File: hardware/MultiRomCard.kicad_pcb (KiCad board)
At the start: 2 copper layers, 125 x 100 mm, 22 parts, among them P1 VC4000_Cartridge_Bus, P2 MicroSD_Breakout, U1 Arduino_Nano, U10 74HC32, U2 74HC595, U3 74HC595, U4 74HC595, U5 6264, U6 74HC245, U7 74HC245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

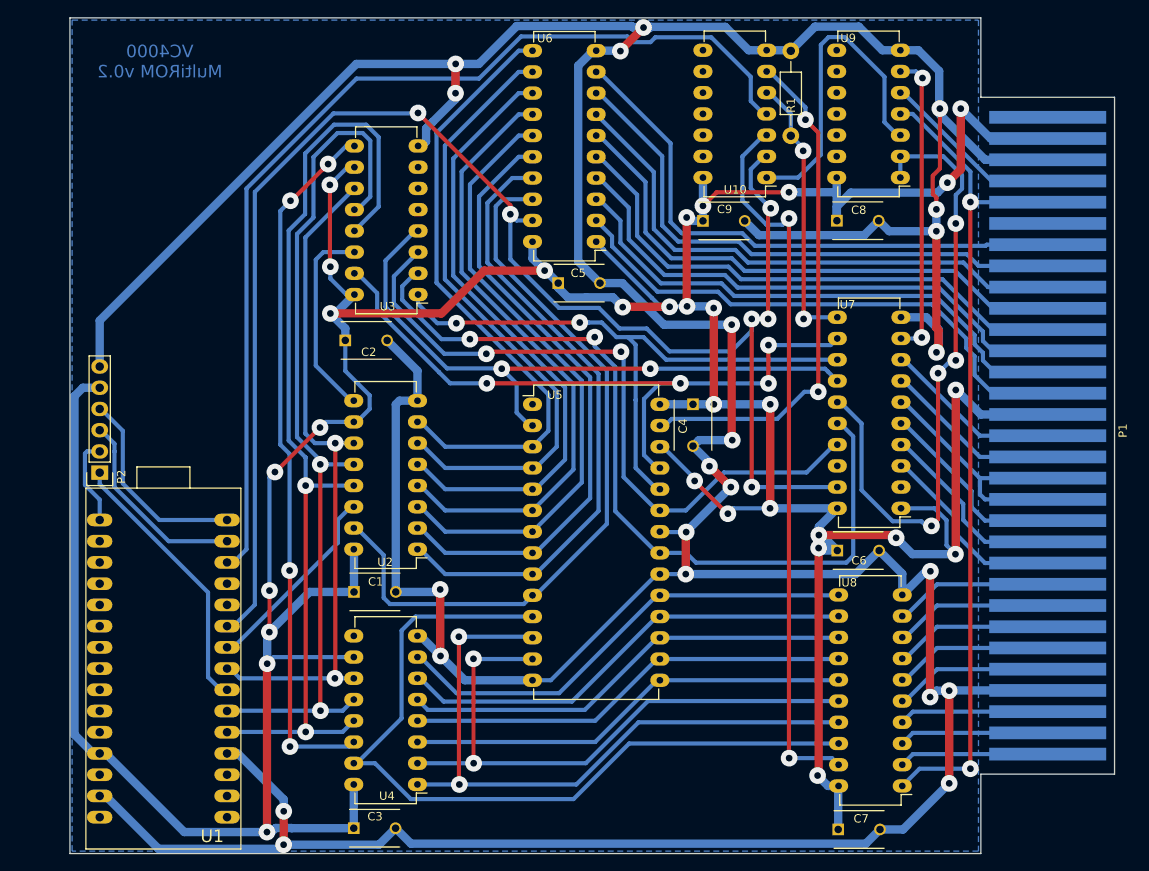
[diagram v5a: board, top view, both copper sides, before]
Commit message: added 3 push buttons and a display prot connected to I2C
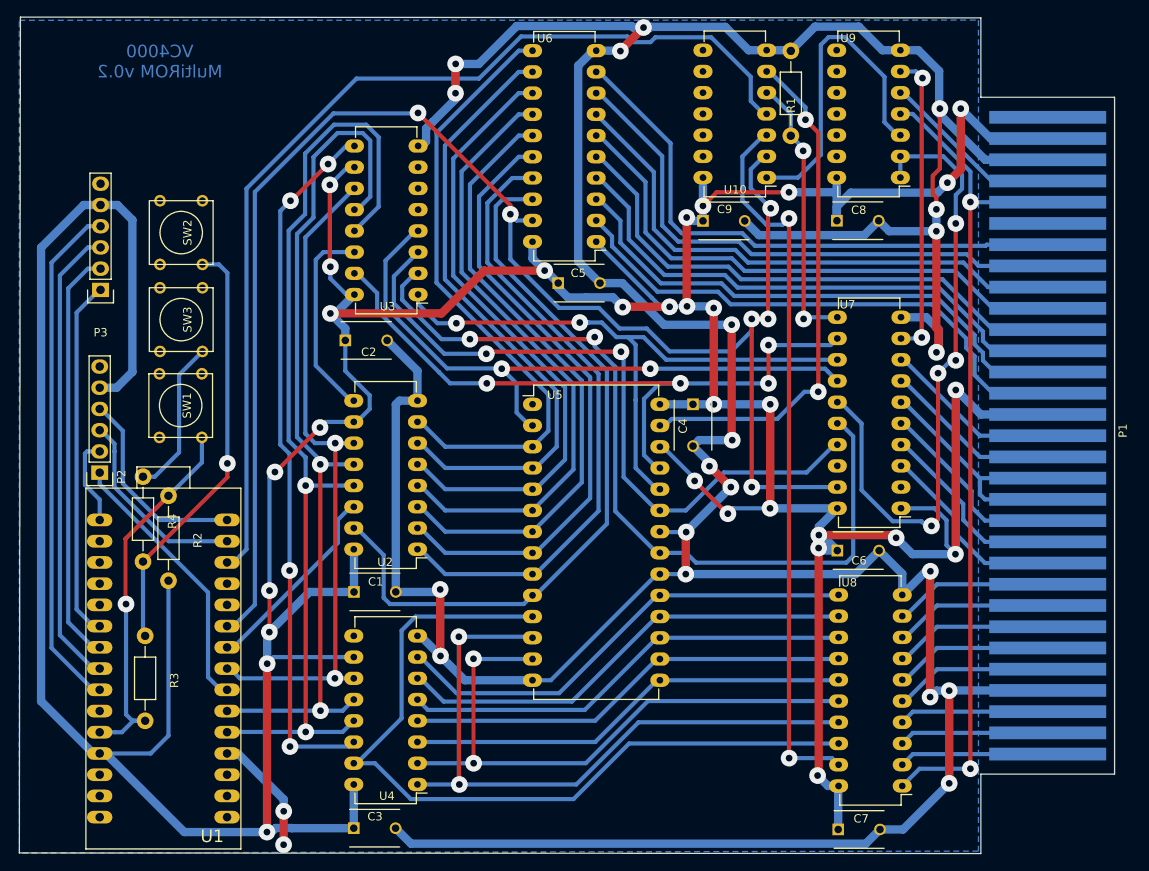
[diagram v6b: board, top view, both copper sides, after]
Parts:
- added P3: DISPLAY, Pin_Headers:Pin_Header_Straight_1x06, F.Cu at (89.7, 81.1)
- added R2: 2k2, Resistors_ThroughHole:Resistor_Horizontal_RM10mm, F.Cu at (97.8, 110.8)
- added R3: 330, Resistors_ThroughHole:Resistor_Horizontal_RM10mm, F.Cu at (95.0, 127.5)
- added R4: 1k, Resistors_ThroughHole:Resistor_Horizontal_RM10mm, F.Cu at (94.7, 108.5)
- added SW1: UP, Buttons_Switches_ThroughHole:SW_PUSH_SMALL, F.Cu at (99.3, 94.9)
- added SW2: DOWN, Buttons_Switches_ThroughHole:SW_PUSH_SMALL, F.Cu at (99.3, 74.2)
- added SW3: SELECT, Buttons_Switches_ThroughHole:SW_PUSH_SMALL, F.Cu at (99.3, 84.6)
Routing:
- net GND: track 603.8 -> 504.7 mm
- net VCC: track 520.2 -> 600.9 mm
- net Net-(P3-Pad4): track 0.00 -> 61.8 mm
- net Net-(P3-Pad3): track 0.00 -> 55.9 mm
- net Net-(R3-Pad1): track 0.00 -> 51.1 mm, vias 0 -> 1
- net Net-(P3-Pad2): track 0.00 -> 49.8 mm
- net Net-(R2-Pad1): track 0.00 -> 45.6 mm, vias 0 -> 1
- net Net-(P3-Pad1): track 0.00 -> 43.1 mm
- net Net-(R4-Pad1): track 0.00 -> 18.8 mm
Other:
- board size 125 x 100 mm -> 131.1 x 100.1 mm

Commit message: increased size of several vias for better soldering
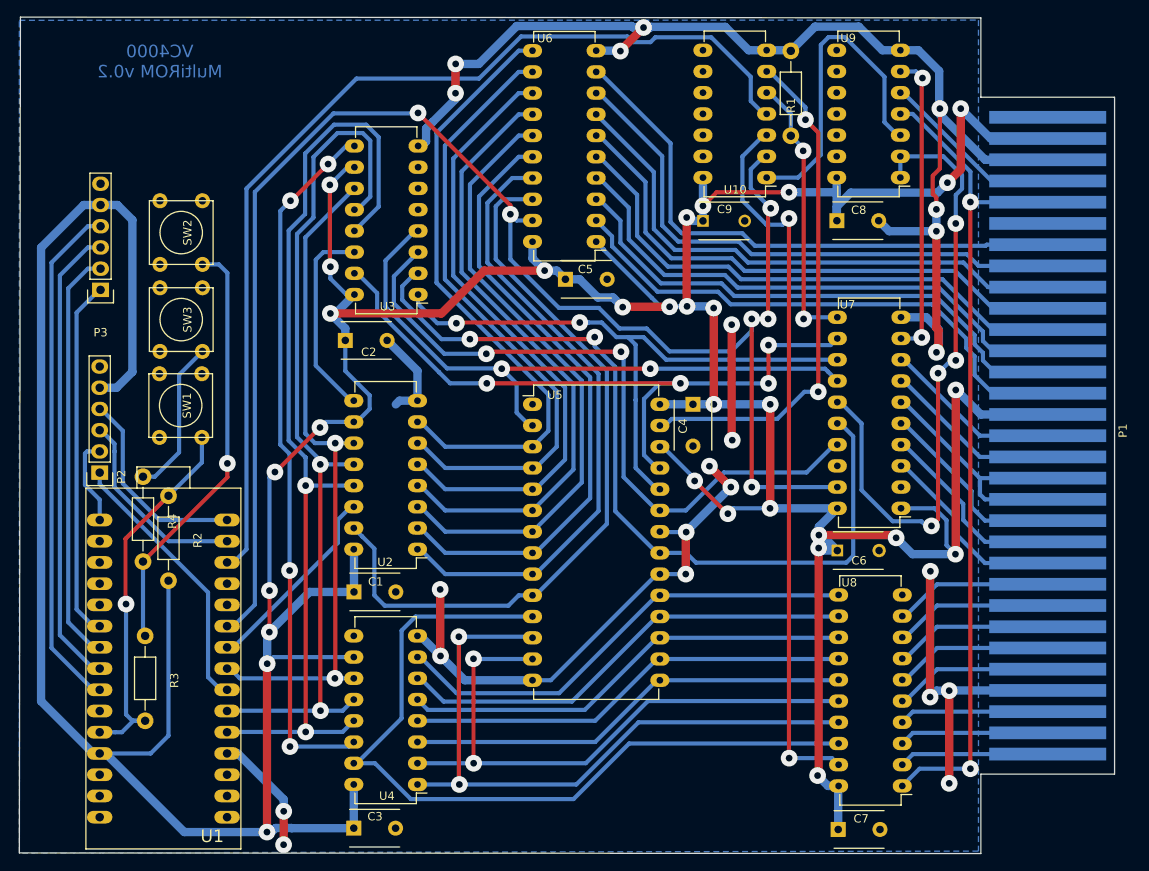
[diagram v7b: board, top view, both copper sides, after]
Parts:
- moved C5 0.98 mm to (145.3, 79.8)
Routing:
- net GND: track 504.7 -> 285.5 mm, vias 22 -> 20
- net (no net): track 0.00 -> 13.9 mm, vias 0 -> 2
- net /A0: track 89.3 -> 90.6 mm

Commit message: [HW] PCB cleanup and new printouts.
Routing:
- net (no net): track 13.9 -> 0.00 mm, vias 2 -> 0
- net Net-(R4-Pad1): track 18.8 -> 26.4 mm
- net Net-(R3-Pad1): track 51.1 -> 58.7 mm
- net Net-(R2-Pad1): track 45.6 -> 53.2 mm
- net GND: track 285.5 -> 281.0 mm
- net VCC: track 600.7 -> 597.8 mm
- net /A0: track 90.6 -> 89.7 mm
- net Net-(P3-Pad4): track 61.8 -> 61.2 mm
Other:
- board size 131.1 x 100.1 mm -> 131.3 x 100 mm
